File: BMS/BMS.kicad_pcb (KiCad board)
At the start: 4 copper layers, 111 x 147 mm, 346 parts, among them IC1 STM32H742VIT6, IC2 TPS563200DDCR, J1 Conn_01x17, J10 Conn_01x10, J11 USB4235-03-C_REVA, J12 Conn_01x17, J13 USB_A, J16 Conn_01x10, J19 Conn_02x13_Counter_Clockwise, J7 FTSH-107-01-L-D-K, Q1 NPN, Q2 NPN, Q5 DMT6018LDR-7, Q7 DMT6018LDR-7, SW1 SW_Push, U1 BQ79614PAPRQ1, U2 BQ79614PAPRQ1, U3 PBQ79600PWQ1, U4 MCP2542FD-E/MF, U5 PTPSM863253RDXR

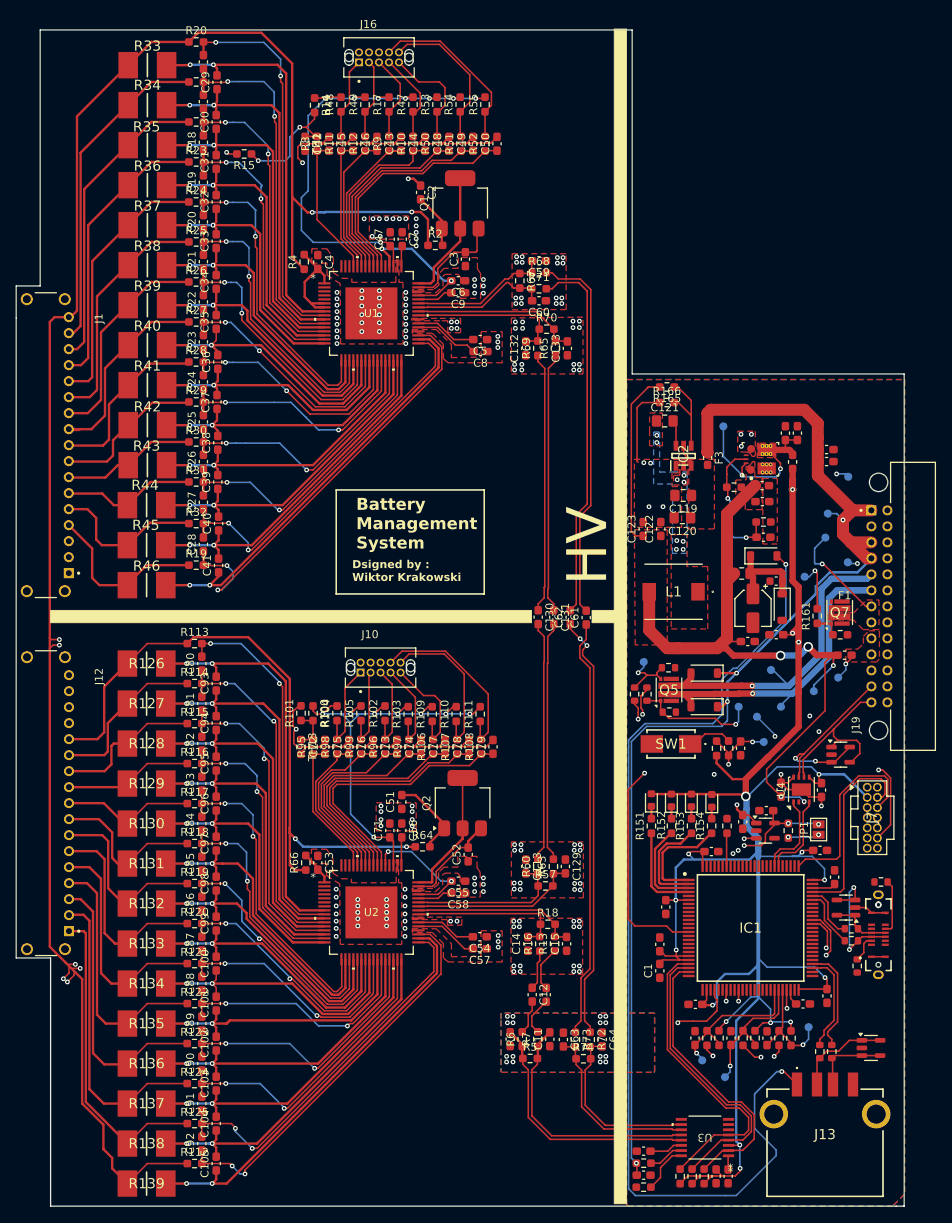
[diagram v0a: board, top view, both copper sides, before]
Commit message: Zmienione kondensatory na kondensatory bezpieczeństwa,poprawiono strefy na thermal relief oraz naprawiono bledy z tym zwiazane, impedancja do zmiany jeszcze
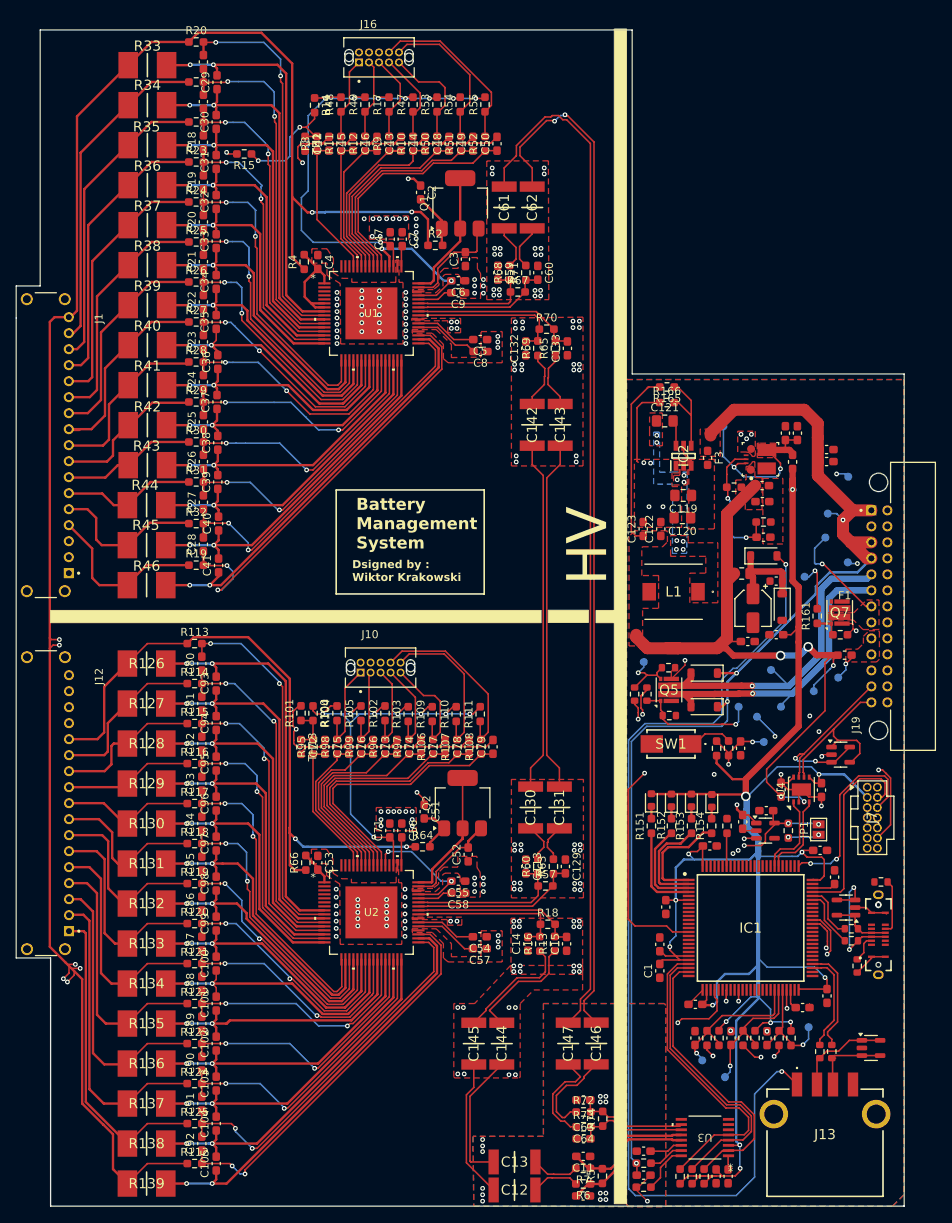
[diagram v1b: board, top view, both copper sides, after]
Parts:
- added C142: 2.2n, footrpint:CAPC5728X280N, F.Cu at (140.4, 87.3)
- added C143: 2.2n, footrpint:CAPC5728X280N, F.Cu at (143.9, 87.3)
- added C144: 2.2n, footrpint:CAPC5728X280N, F.Cu at (136.6, 164.6)
- added C145: 2.2n, footrpint:CAPC5728X280N, F.Cu at (133.1, 164.6)
- added C146: 2.2n, footrpint:CAPC5728X280N, F.Cu at (148.4, 164.6)
- added C147: 2.2n, footrpint:CAPC5728X280N, F.Cu at (144.9, 164.6)
- C12, C13, C130, C131, C61, C62: footprint Capacitor_SMD:C_0603_1608Metric_Pad1.08x0.95mm_HandSolder -> footrpint:CAPC5728X280N
- moved C61 52.3 mm to (136.9, 60.1), turned to -90 degrees
- moved C62 51.4 mm to (140.4, 60.1), turned to -90 degrees
- moved C12 24.5 mm to (138.2, 182.9), turned to 0 degrees
- moved C130 23.8 mm to (140.2, 135.1)
- moved C131 23.8 mm to (143.8, 135.1)
- moved C10 21.6 mm to (146.8, 183.7), turned to 180 degrees
- moved C13 21.3 mm to (138.2, 179.4), turned to 0 degrees
- moved R6 19.6 mm to (146.8, 182.2), turned to 180 degrees
- moved R5 17.3 mm to (149.2, 181.2), turned to 90 degrees
- moved R7 17.1 mm to (146.8, 180.2), turned to 180 degrees
- moved C11 15.2 mm to (146.8, 178.7), turned to 180 degrees
- moved C63 12.7 mm to (146.8, 176.5), turned to 0 degrees
- moved R73 10.9 mm to (146.8, 175.0), turned to 0 degrees
- moved R72 9.09 mm to (146.8, 173.2), turned to 0 degrees
- moved C64 7.92 mm to (146.8, 171.7), turned to 0 degrees
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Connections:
- R13 pad 1: /galvanic_isulation_2/S2- -> /galvanic_isulation_2/S3-
- R16 pad 1: /galvanic_isulation_2/S2+ -> /galvanic_isulation_2/S3+
- R65 pad 1: /galvanic_isulation_1/S2- -> /galvanic_isulation_1/S3-
- R69 pad 1: /galvanic_isulation_1/S2+ -> /galvanic_isulation_1/S3+
- R72 pad 1: /galvanic_isulation_0/S2- -> /galvanic_isulation_0/S3-
- R73 pad 1: /galvanic_isulation_0/S2+ -> /galvanic_isulation_0/S3+
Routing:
- net /galvanic_isulation_0/S2+: track 52.6 -> 129.1 mm
- net /galvanic_isulation_0/S2-: track 53.4 -> 129.2 mm
- net /galvanic_isulation_0/S1+: track 47.5 -> 5.57 mm
- net /galvanic_isulation_0/S1-: track 46.7 -> 5.61 mm
- net /galvanic_isulation_1/S1-: track 30.0 -> 4.78 mm
- net /galvanic_isulation_1/S1+: track 30.0 -> 4.84 mm
- net GND: track 27.4 -> 50.8 mm, vias 26 -> 30
- net /galvanic_isulation_2/S3-: track 0.00 -> 14.6 mm
- net /galvanic_isulation_2/S3+: track 0.00 -> 14.6 mm
- net /STM Comunication Interface /COMHP: track 31.9 -> 17.4 mm
- net /STM Comunication Interface /COMHN: track 31.1 -> 16.7 mm
- net /galvanic_isulation_0/S3+: track 0.00 -> 12.5 mm
- net /galvanic_isulation_2/S2+: track 4.97 -> 17.5 mm
- net /galvanic_isulation_0/S3-: track 0.00 -> 11.8 mm
- net /galvanic_isulation_1/S2-: track 32.6 -> 44.0 mm
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- added copper zone on F.Cu, net +12V
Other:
- outline, holes or cut-outs redrawn
